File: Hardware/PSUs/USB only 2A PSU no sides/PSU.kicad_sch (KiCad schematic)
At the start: 14 parts, among them U1 AP63205WU, U2 AP63203WU, U7 TPS7A2633DRV

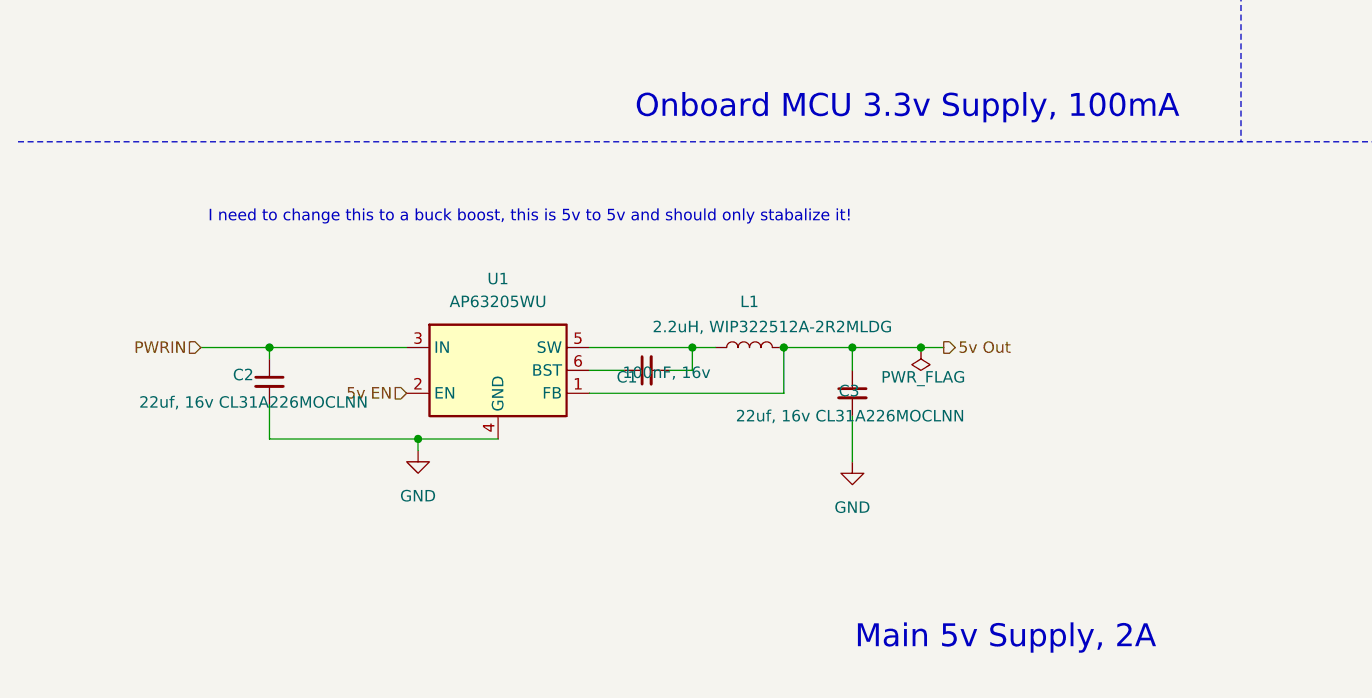
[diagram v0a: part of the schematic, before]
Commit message: Finished schematic, started arrangement
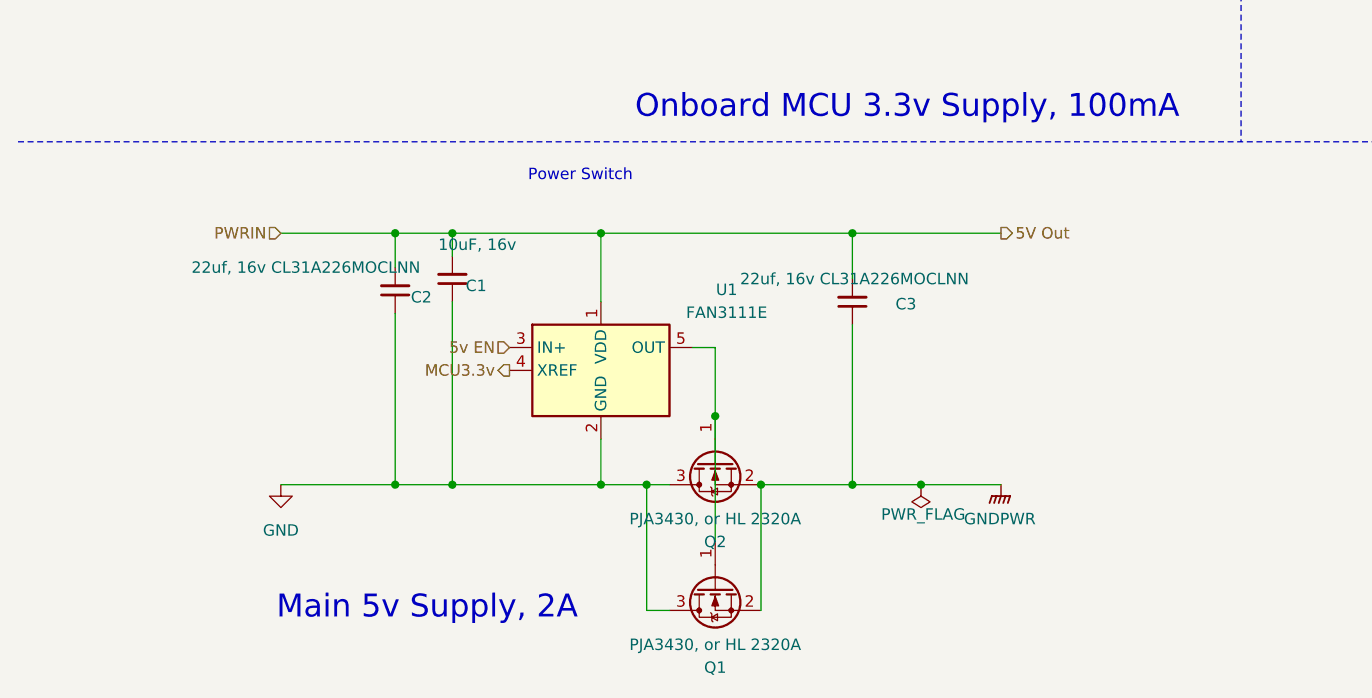
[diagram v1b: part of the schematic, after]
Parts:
- removed L1: 2.2uH, WIP322512A-2R2MLDG, Inductor_SMD:L_1008_2520Metric, symbol Device:L
- removed U1: AP63205WU, Package_TO_SOT_SMD:TSOT-23-6, symbol Regulator_Switching:AP63203WU
- added Q1, Q2: PJA3430, or HL 2320A, Package_TO_SOT_SMD:SC-59, symbol Device:Q_NMOS_GSD
- added U1: FAN3111E, Package_TO_SOT_SMD:SOT-23-5, symbol Driver_FET:FAN3111E
- C1: value 100nF, 16v -> 10uF, 16v; LCSC C14663 -> C96446
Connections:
- net 5v EN: now also U1.3 (IN+)
- net GND: now also C1.1, C2.1, Q1.3 (D), Q2.3 (D), U1.2 (GND); no longer C2.2, C3.2
- net MCU3.3v: now also U1.4 (XREF)
- net 5V Out: now reaches C1.2
- net 5V Out: now also C2.2, C28.1, C3.2, U2.3 (IN), U1.1 (VDD)
- net 5v Out renamed GNDPWR
- net GNDPWR: now also Q1.2 (S), Q2.2 (S)
- removed net PWRIN: C2.1, C28.1, U2.3 (IN)
- new net: Q1.1 (G), Q2.1 (G), U1.5 (OUT)
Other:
- note added: "Power Switch"
- note removed: "I need to change this to a buck boost, this is 5v to 5v and should only stabalize it!"
- moved on the sheet: C2, C3

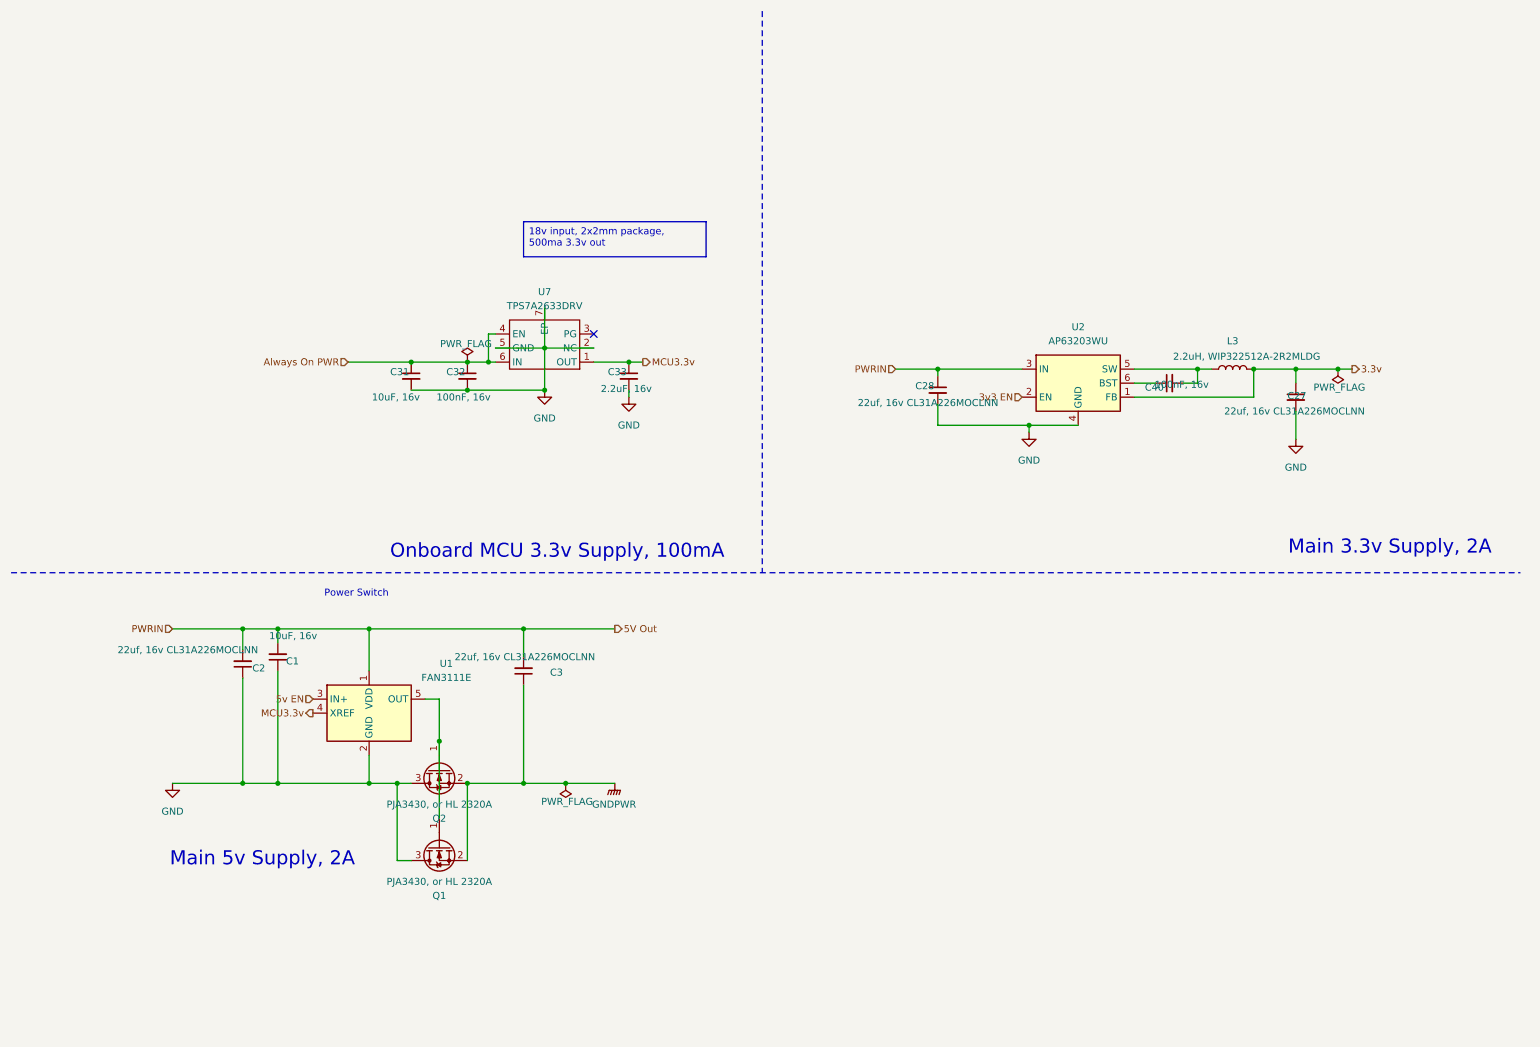
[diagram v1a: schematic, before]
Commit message: Moved current sense to PSU schematic
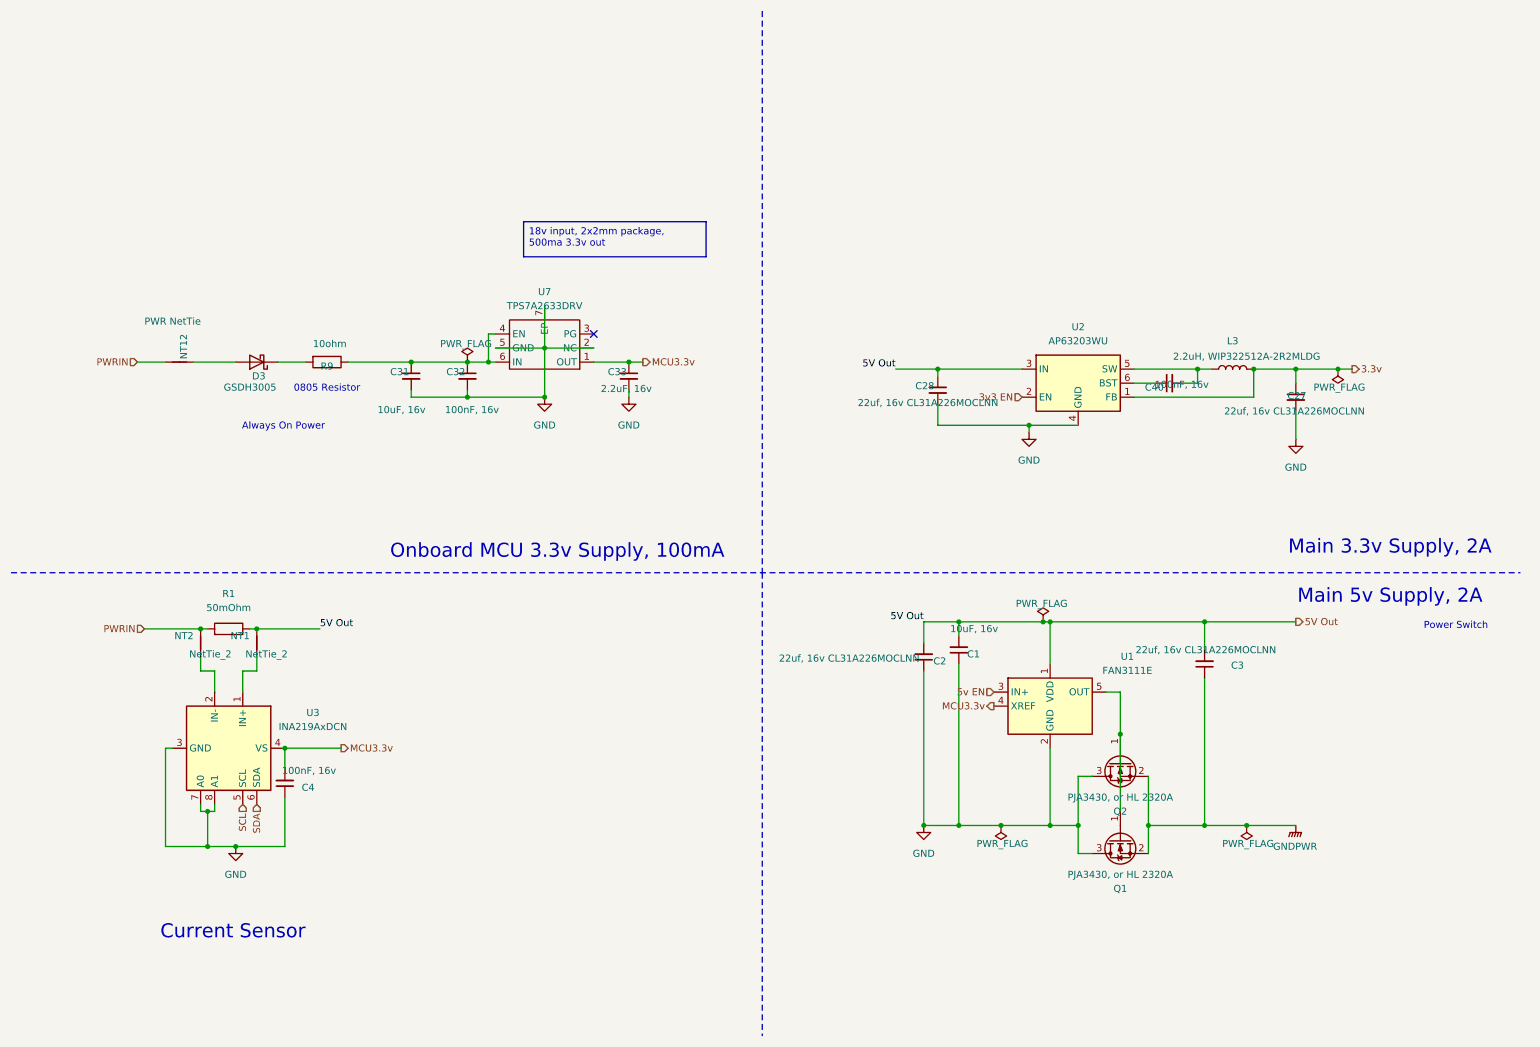
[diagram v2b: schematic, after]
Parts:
- added C4: 100nF, 16v, Capacitor_SMD:C_0805_2012Metric, symbol Device:C_Small
- added D3: GSDH3005, Diode_SMD:D_0402_1005Metric, symbol Device:D_Schottky
- added NT1, NT2: NetTie_2, custom_Connector:NetTie-2_SMD_Pad0.2mm, symbol Device:NetTie_2
- added NT12: PWR NetTie, custom_Connector:NetTie-2_SMD_Pad0.28mm, symbol Device:NetTie_2
- added R1: 50mOhm, Resistor_SMD:R_2512_6332Metric, symbol Device:R
- added R9: 10ohm, Resistor_SMD:R_0805_2012Metric, symbol Device:R
- added U3: INA219AxDCN, Package_TO_SOT_SMD:SOT-23-8, symbol Sensor_Energy:INA219AxDCN
- C1, C31, C40: footprint Capacitor_SMD:C_0603_1608Metric -> Capacitor_SMD:C_0805_2012Metric
- C32, C33: footprint Capacitor_SMD:C_0402_1005Metric -> Capacitor_SMD:C_0805_2012Metric
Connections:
- net 5V Out: now also NT1.2, R1.1
- net GND: now also C4.1, U3.3 (GND), U3.7 (A0), U3.8 (A1)
- net MCU3.3v: now also C4.2, U3.4 (VS)
- net Always On PWR: no longer names the net of C31.1, C32.1, U7.4 (EN), U7.6 (IN)
- net Always On PWR: now also R9.1
- new net: NT1.1, U3.1 (IN+)
- new net: NT2.1, U3.2 (IN-)
- new net: D3.1 (K), R9.2
- new net: D3.2 (A), NT12.1
- new net PWRIN: NT12.2, NT2.2, R1.2
- new net SCL: U3.5 (SCL)
- new net SDA: U3.6 (SDA)
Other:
- note added: "0805 Resistor"
- note added: "Always On Power"
- note added: "Current Sensor"
- moved on the sheet: C1, C2, C3, Q1, Q2, U1
